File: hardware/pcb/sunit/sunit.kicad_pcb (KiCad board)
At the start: 4 copper layers, 62.2 x 21.6 mm, 41 parts, among them J1 Power, J2 Control, J3 BUS, J4 Input A, J5 Flags, J6 Input B, U5 74HC125, U6 74HC157, U7 74HC157, U8 74HC245

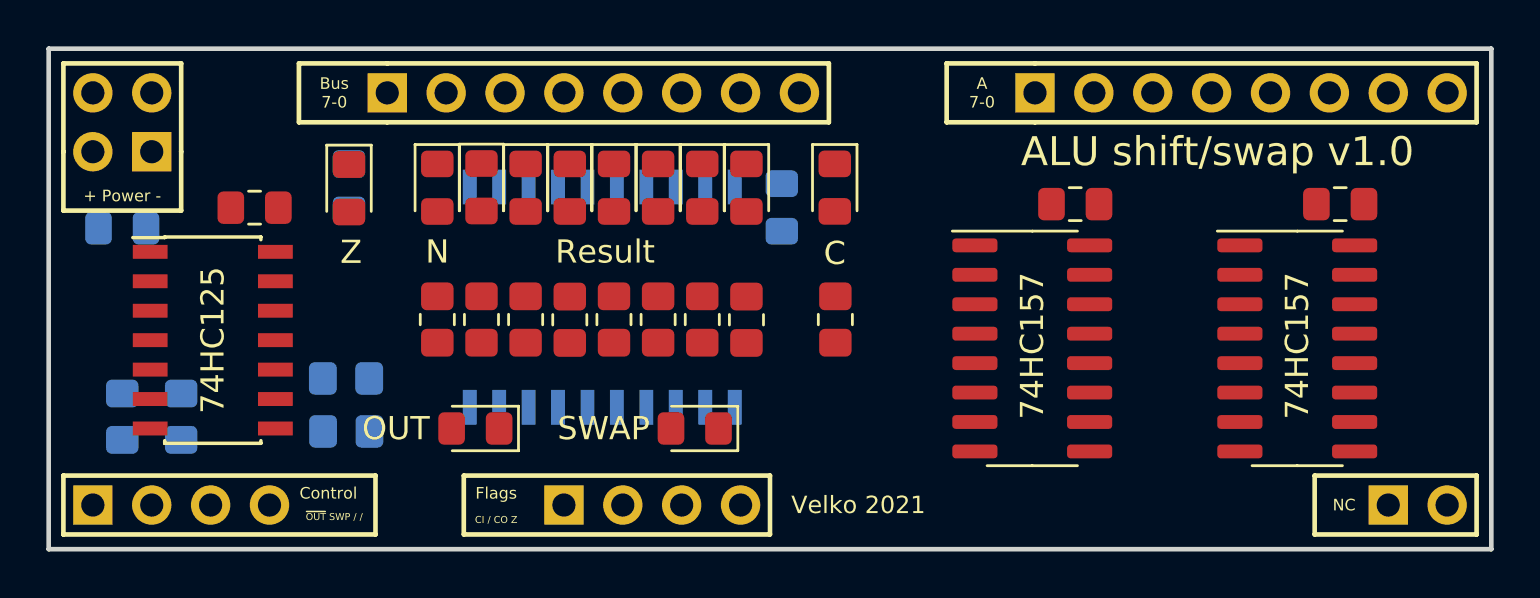
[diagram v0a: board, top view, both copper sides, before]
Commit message: Routed Shift unit
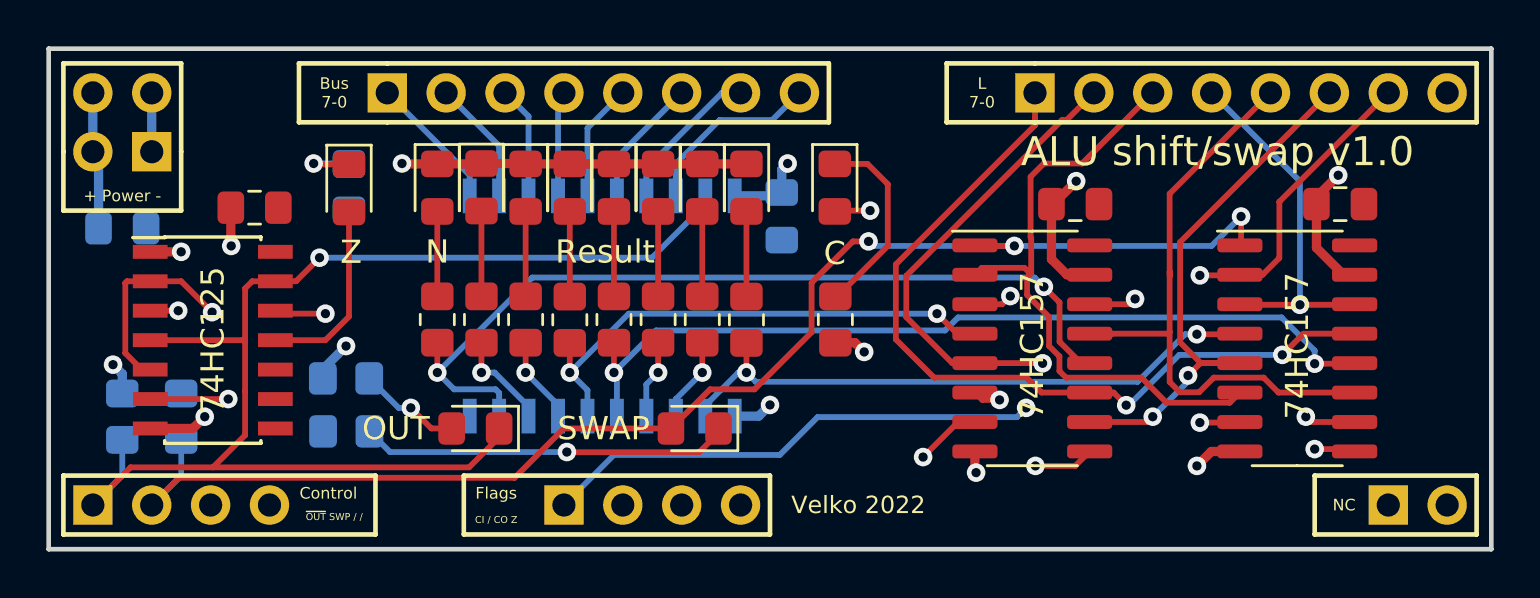
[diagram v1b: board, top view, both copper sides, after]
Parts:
- moved C2 0.38 mm to (66.5, 43.4)
- moved U8 0.38 mm to (58.8, 47.3)
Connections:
- J2 pad 3: Net-(J2-Pad3) -> (no net)
- J2 pad 4: Net-(J2-Pad4) -> (no net)
- J5 pad 2: Net-(J5-Pad2) -> (no net)
- J6 pad 1: Net-(J6-Pad1) -> (no net)
- J6 pad 2: Net-(J6-Pad2) -> (no net)
- U5 pad 10: ~OUT~ -> VCC
- U5 pad 11: Net-(U5-Pad11) -> Net-(D11-Pad2)
- U5 pad 12: VCC -> ZIN
- U5 pad 13: VCC -> ~OUT~
- U5 pad 8: Net-(D11-Pad2) -> (no net)
- U5 pad 9: ZIN -> VCC
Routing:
- net A0: track 0.00 -> 67.6 mm, vias 0 -> 2
- net SH_SWP: track 0.00 -> 59.9 mm, vias 0 -> 3
- net ~OUT~: track 0.00 -> 56.6 mm, vias 0 -> 1
- net GND: track 0.00 -> 38.9 mm, vias 0 -> 9
- net RES7: track 0.00 -> 37.7 mm, vias 0 -> 2
- net RES3: track 0.00 -> 37.3 mm, vias 0 -> 2
- net A7: track 0.00 -> 35.4 mm, vias 0 -> 2
- net RES2: track 0.00 -> 34.8 mm, vias 0 -> 2
- net A6: track 0.00 -> 34.7 mm, vias 0 -> 2
- net Net-(D12-Pad2): track 0.00 -> 34.4 mm, vias 0 -> 2
- net RES6: track 0.00 -> 33.3 mm, vias 0 -> 2
- net CIN: track 0.00 -> 31.8 mm, vias 0 -> 2
- net RES1: track 0.00 -> 28.1 mm, vias 0 -> 2
- net A3: track 0.00 -> 27.6 mm
- net A5: track 0.00 -> 27.0 mm
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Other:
- net class Power added: clearance 0.2, trace_width 0.4, via_dia 0.8, via_drill 0.4
- board text added: "L 7-0"
- board text added: "Velko 2022"
- board text removed: "A 7-0"
- board text removed: "Velko 2021"

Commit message: Finished Shift unit
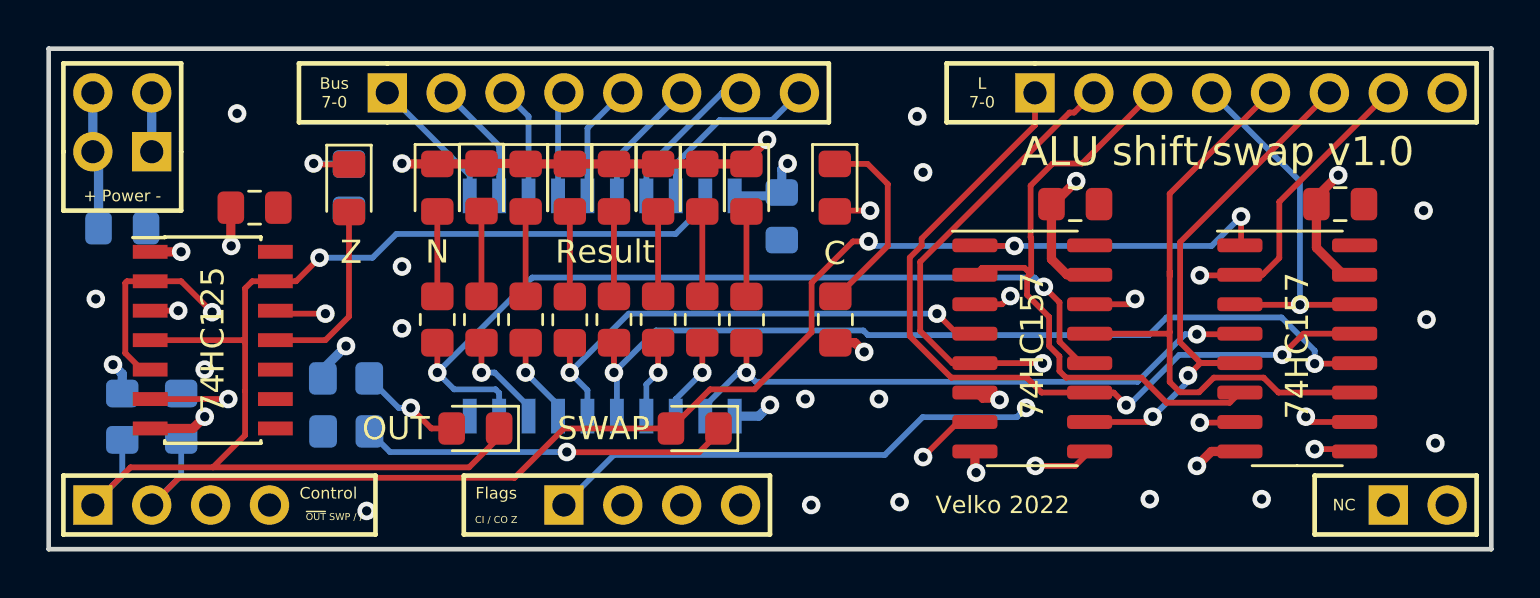
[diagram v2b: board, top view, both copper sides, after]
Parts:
- R11: value 330 -> 1K
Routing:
- net GND: track 38.9 -> 40.3 mm, vias 9 -> 20
- net A7: track 35.4 -> 34.4 mm
- net VCC: vias 4 -> 11
